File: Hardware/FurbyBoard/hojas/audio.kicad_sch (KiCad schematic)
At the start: 8 parts, among them J5 Micro I2S (3V3, GND, SCK, WS,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, U7 MAX98357AETE+T

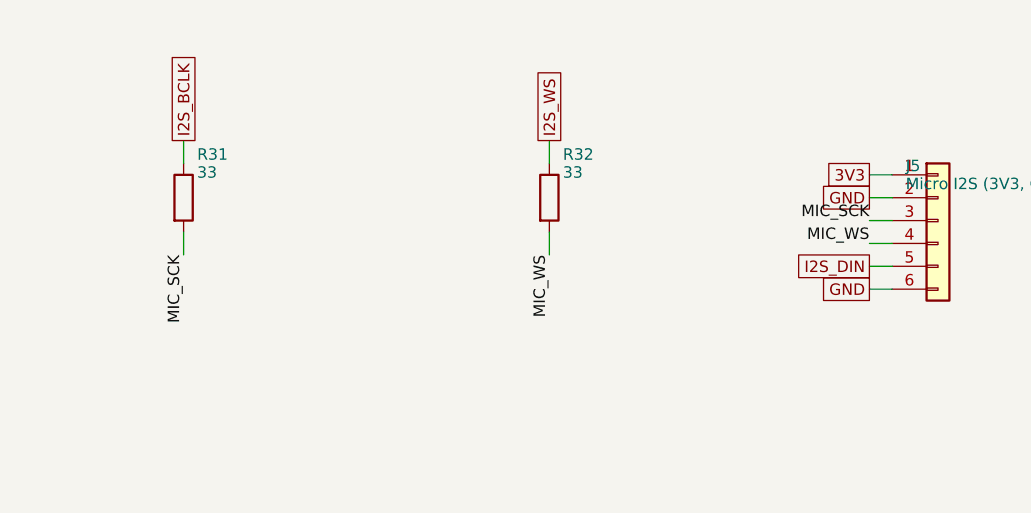
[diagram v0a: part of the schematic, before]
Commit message: Refactor: pads de cable agrupados por zona y etiquetas globales
- Motor en J9 con leva, encoder y sensores; altavoz en J8 con inclinación y
  lengua; luz en J7 con el IR. Desaparecen J4 y J10: cada grupo sale por el
  borde más cercano a su destino.
- Micro en 2x03 en vez de 1x06 para que quepa junto al borde derecho.
- Todas las etiquetas del esquemático son globales, así el nombre de red
  coincide con el del PCB (paridad sin prefijos de hoja).
- ERC 0 errores, 0 avisos.

Co-Authored-By: Claude Opus 5.5 (1M context) <noreply@anthropic.com>
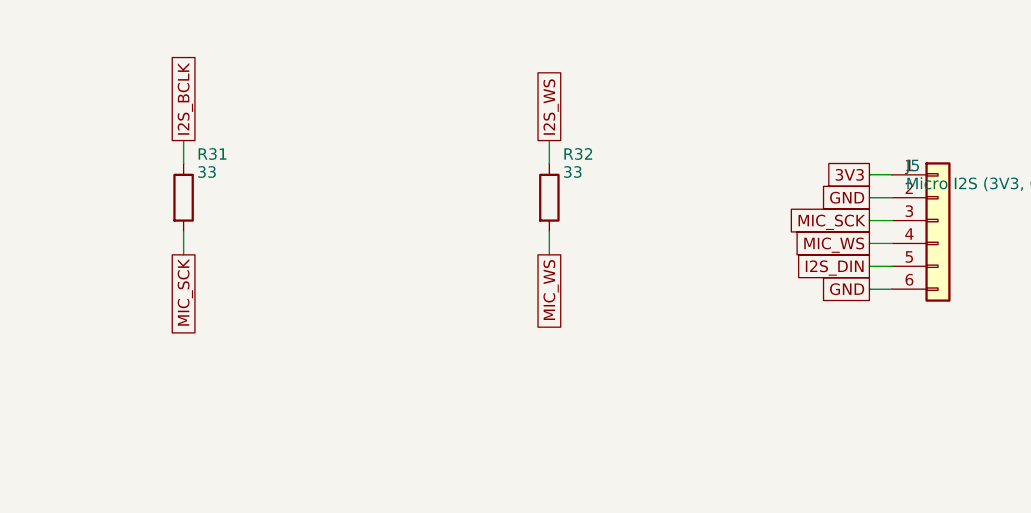
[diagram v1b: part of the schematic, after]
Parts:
- J5: footprint FurbyBoard:Pads_1x06_P2.54mm -> FurbyBoard:Pads_2x03_P2.54mm

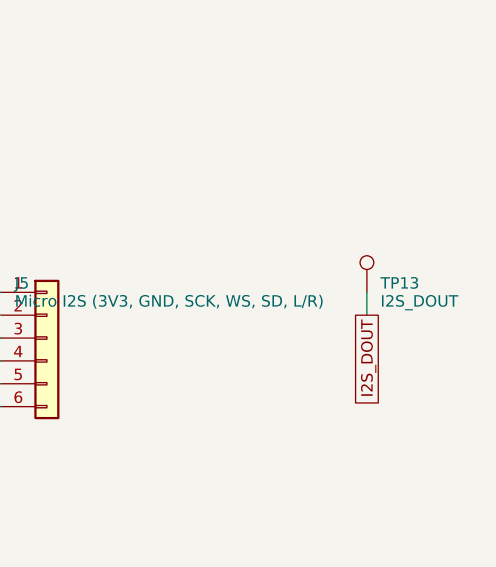
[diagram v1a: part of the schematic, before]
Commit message: Feature: par USB trazado, planos GND/VSYS y serigrafía de la FurbyBoard
- Par USB de J1 al ESD y al módulo, acoplado 0,28/0,15 por F.Cu sobre el
  plano de GND, sin vías (rutas_fijas.py, bloqueado para el autorrutado).
  Canal libre en x -83 bajo la batería.
- In1 plano de GND e In2 plano de VSYS; potencia por pista a 0,4 (cabe en
  los pads de 0,5 de paso) y 3V3 a 0,3. exportar_dsn.py deja el DSN para
  Freerouting con las clases de red.
- Rótulos de serigrafía colocados solos (serigrafia.py): TP, LED, botones,
  puentes y polaridad de la batería arriba; función de cada pad de cable y
  GPIO del J_EXP abajo, con leyenda para J7, J9 y J5.
- Para que quepan los rótulos: fila de LED con resistencias debajo, botones
  en vertical, rejilla de TP con el rótulo debajo. Quedan 14 TP: fuera EN e
  IO0 (se miden en los pads de SW1 y SW2), CHG y PG (en D1 y D2) y un GND.

ERC 0/0. DRC 0 salvo una vía de GND sin plano relleno; sin rutar.

Co-Authored-By: Claude Opus 5.5 (1M context) <noreply@anthropic.com>
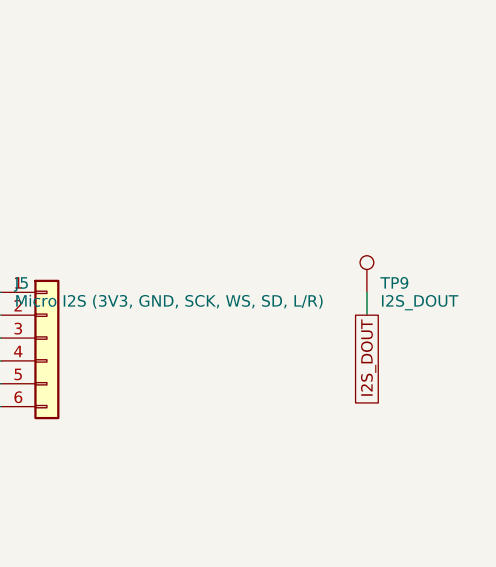
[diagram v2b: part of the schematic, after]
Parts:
- removed TP13: I2S_DOUT, TestPoint:TestPoint_Pad_D1.5mm, symbol Connector:TestPoint
- added TP9: I2S_DOUT, TestPoint:TestPoint_Pad_D1.5mm, symbol Connector:TestPoint
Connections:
- net I2S_DOUT: now also TP9.1
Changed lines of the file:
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@@
-	)
-	(symbol
-		(lib_id "Connector:TestPoint")
-		(at 353.06 66.04 0)
-		(unit 1)
-		(body_style 1)
-		(exclude_from_sim no)
-		(in_bom no)
-		(on_board yes)
-		(in_pos_files yes)
-		(dnp no)
-		(property "Reference" "TP13"
-			(at 354.56 65.04 0)
-			(show_name no)
-			(do_not_autoplace no)
-			(effects
-				(font
-					(size 1.27 1.27)
-				)
-				(justify left)
-			)
-		)
-		(property "Value" "I2S_DOUT"
-			(at 354.56 67.04 0)
-			(show_name no)
-			(do_not_autoplace no)
-			(effects
-				(font
-					(size 1.27 1.27)
-				)
-				(justify left)
-			)
-		)
-		(property "Footprint" "TestPoint:TestPoint_Pad_D1.5mm"
-			(at 353.06 66.04 0)
-			(hide yes)
-			(show_name no)
-			(do_not_autoplace no)
-			(effects
-				(font
-					(size 1.27 1.27)
-				)
-				(justify left)
-			)
-		)
-		(property "Datasheet" ""
-			(at 353.06 66.04 0)
-			(hide yes)
-			(show_name no)
-			(do_not_autoplace no)
-			(effects
-				(font
-					(size 1.27 1.27)
-				)
-				(justify left)
-			)
-		)
-		(property "Description" "Datos I2S al amplificador"
-			(at 353.06 66.04 0)
-			(hide yes)
-			(show_name no)
-			(do_not_autoplace no)
-			(effects
-				(font
-					(size 1.27 1.27)
-				)
-				(justify left)
-			)
-		)
-		(property "LCSC" ""
-			(at 353.06 66.04 0)
-			(hide yes)
-			(show_name no)
-			(do_not_autoplace no)
-			(effects
-				(font
-					(size 1.27 1.27)
-				)
-				(justify left)
-			)
-		)
-		(property "JLC_Class" ""
-			(at 353.06 66.04 0)
-			(hide yes)
-			(show_name no)
-			(do_not_autoplace no)
-			(effects
-				(font
-					(size 1.27 1.27)
-				)
-				(justify left)
-			)
-		)
-		(property "MPN" ""
-			(at 353.06 66.04 0)
-			(hide yes)
-			(show_name no)
-			(do_not_autoplace no)
-			(effects
-				(font
-					(size 1.27 1.27)
-				)
-				(justify left)
-			)
-		)
-		(pin "1"
-		)
-		(instances
-			(project "FurbyBoard"
-				(path "/8b4f1e2a-3c5d-4e6f-9a1b-2c3d4e5f6a7b/259e0c7a-58f0-5f84-8b75-920a4cd1054d"
-					(reference "TP13")
-					(unit 1)
-				)
-			)
-		)
 	)
 	(symbol
@@
 					(unit 1)
 				)
+			)
+		)
+	)
+	(symbol
+		(lib_id "Connector:TestPoint")
+		(at 353.06 66.04 0)
+		(unit 1)
+		(body_style 1)
+		(exclude_from_sim no)
+		(in_bom no)
+		(on_board yes)
+		(in_pos_files yes)
+		(dnp no)
+		(property "Reference" "TP9"
+			(at 354.56 65.04 0)
+			(show_name no)
+			(do_not_autoplace no)
+			(effects
+				(font
+					(size 1.27 1.27)
+				)
+				(justify left)
+			)
+		)
+		(property "Value" "I2S_DOUT"
+			(at 354.56 67.04 0)
+			(show_name no)
+			(do_not_autoplace no)
+			(effects
+				(font
+					(size 1.27 1.27)
+				)
+				(justify left)
+			)
+		)
+		(property "Footprint" "TestPoint:TestPoint_Pad_D1.5mm"
+			(at 353.06 66.04 0)
+			(hide yes)
+			(show_name no)
+			(do_not_autoplace no)
+			(effects
+				(font
+					(size 1.27 1.27)
+				)
+				(justify left)
+			)
+		)
+		(property "Datasheet" ""
+			(at 353.06 66.04 0)
+			(hide yes)
+			(show_name no)
+			(do_not_autoplace no)
+			(effects
+				(font
+					(size 1.27 1.27)
+				)
+				(justify left)
+			)
+		)
+		(property "Description" "Datos I2S al amplificador"
+			(at 353.06 66.04 0)
+			(hide yes)
+			(show_name no)
+			(do_not_autoplace no)
+			(effects
+				(font
+					(size 1.27 1.27)
+				)
+				(justify left)
+			)
+		)
+		(property "LCSC" ""
+			(at 353.06 66.04 0)
+			(hide yes)
+			(show_name no)
+			(do_not_autoplace no)
+			(effects
+				(font
+					(size 1.27 1.27)
+				)
+				(justify left)
+			)
+		)
+		(property "JLC_Class" ""
+			(at 353.06 66.04 0)
+			(hide yes)
+			(show_name no)
+			(do_not_autoplace no)
+			(effects
+				(font
+					(size 1.27 1.27)
+				)
+				(justify left)
+			)
+		)
+		(property "MPN" ""
+			(at 353.06 66.04 0)
+			(hide yes)
+			(show_name no)
+			(do_not_autoplace no)
+			(effects
+				(font
+					(size 1.27 1.27)
+				)
+				(justify left)
+			)
+		)
+		(pin "1"
+		)
+		(instances
+			(project "FurbyBoard"
+				(path "/8b4f1e2a-3c5d-4e6f-9a1b-2c3d4e5f6a7b/259e0c7a-58f0-5f84-8b75-920a4cd1054d"
+					(reference "TP9")
+					(unit 1)
+				)

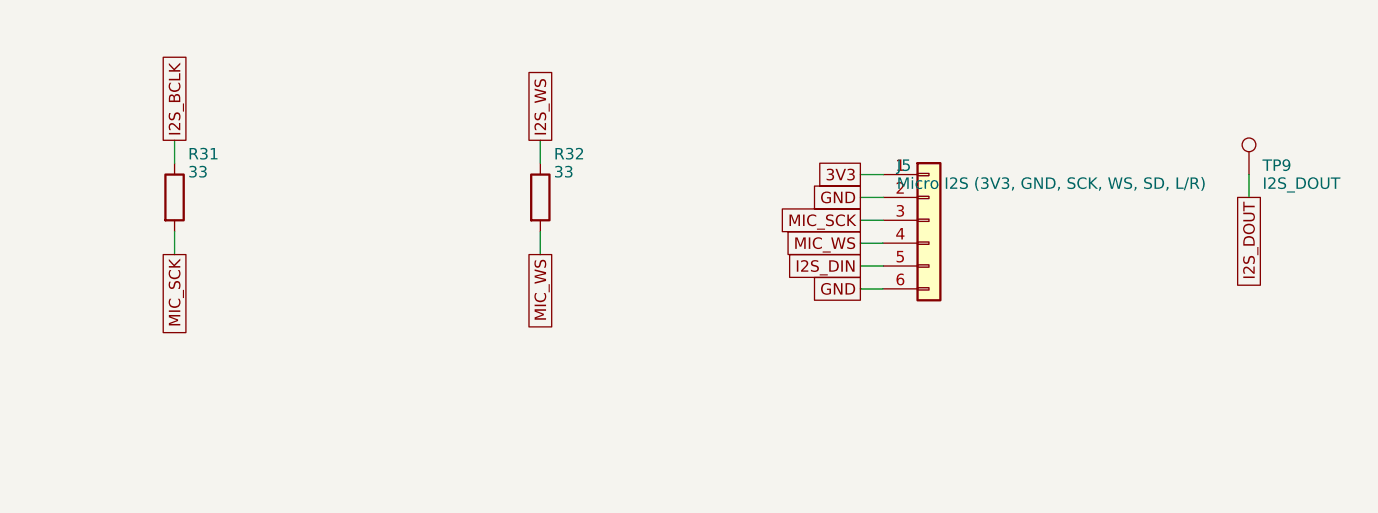
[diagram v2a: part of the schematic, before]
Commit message: Feature: esquema de la FurbyBoard al procedimiento nuevo: rúbrica L, reglas por red, pines por geometría y simulación del elevador
- Rúbrica S/M/L (L) y tabla de raíles con anchos mínimos (params.ANCHOS_MINIMOS), que gen_pro.py vuelca al .kicad_dru como una regla por red, con cuellos dentro de los patios de los QFN y de J1.
- Vías de 0,45/0,2 solo en la clase USB (cruce del par en el receptáculo de 16 pines); el resto sigue en 0,6/0,3.
- pcb-toolkit.toml: clases B/C/D, anchos, grupos explícitos y zonas del puente H y de la clase D.
- Redes a la convención: BB_SW1/2, I2S_SCK_MIC/I2S_WS_MIC.
- Pines del módulo (I2S, HOME, EXP_INT) y puertos del TCA9535 por geometría, sin tocar strapping, USB ni ADC.
- LED del encoder desde V6 por 470 ohm (sin Q2); J_EXP 2x5; J9 y J5 reordenados; serigrafía al día.
- ERC 0/0. Simulación ngspice del elevador en el peor caso (sim/). Informes de las puertas A y B en revisiones/; un crítico (NTC del cargador) queda escalado.

Co-Authored-By: Claude Fable 5.1 <noreply@anthropic.com>
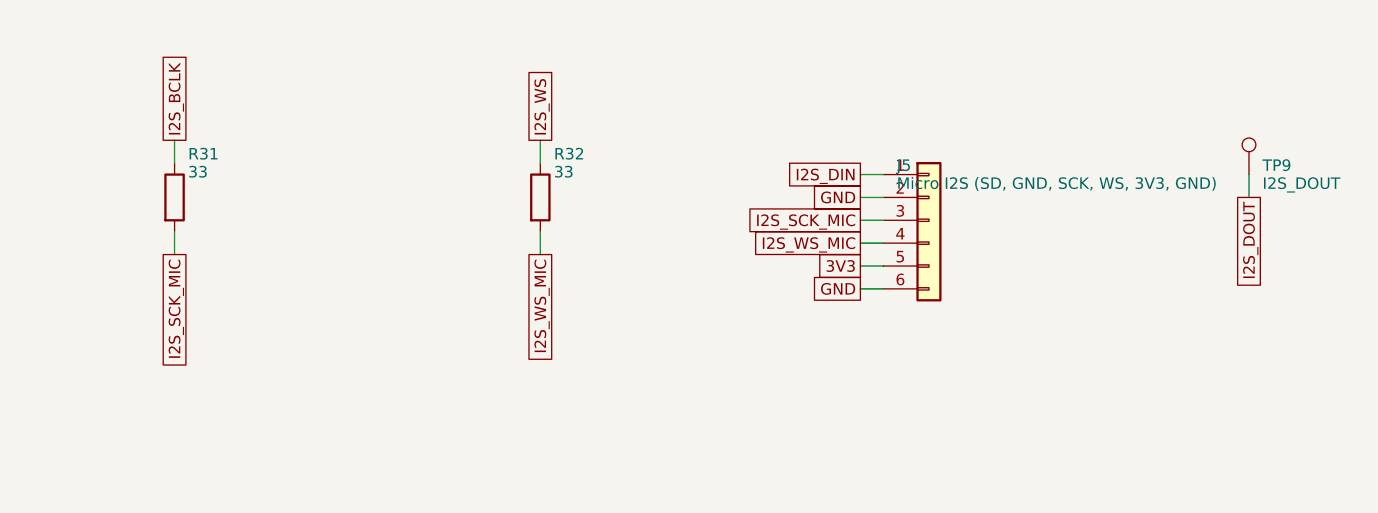
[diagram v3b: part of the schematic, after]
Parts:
- J5: value Micro I2S (3V3, GND, SCK, WS, SD, L/R) -> Micro I2S (SD, GND, SCK, WS, 3V3, GND)
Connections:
- net 3V3: now also J5.5 (Pin_5); no longer J5.1 (Pin_1)
- net I2S_DIN: now also J5.1 (Pin_1); no longer J5.5 (Pin_5)
- net MIC_SCK renamed I2S_SCK_MIC
- net MIC_WS renamed I2S_WS_MIC
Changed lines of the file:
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@@
 		)
 	)
-	(global_label "MIC_SCK"
+	(global_label "I2S_SCK_MIC"
 		(shape passive)
 		(at 233.68 74.93 270)
@@
 		)
 	)
-	(global_label "MIC_SCK"
+	(global_label "I2S_SCK_MIC"
 		(shape passive)
 		(at 309.88 71.12 180)
@@
 		)
 	)
-	(global_label "MIC_WS"
+	(global_label "I2S_WS_MIC"
 		(shape passive)
 		(at 274.32 74.93 270)
@@
 		)
 	)
-	(global_label "MIC_WS"
+	(global_label "I2S_WS_MIC"
 		(shape passive)
 		(at 309.88 73.66 180)
@@
 		)
 	)
+	(global_label "3V3"
+		(shape passive)
+		(at 309.88 76.2 180)
+		(fields_autoplaced yes)
+		(effects
+			(font
+				(size 1.27 1.27)
+			)
+			(justify right)
+		)
+		(property "Intersheetrefs" "${INTERSHEET_REFS}"
+			(at 309.88 76.2 0)
+			(hide yes)
+			(show_name no)
+			(do_not_autoplace no)
+			(effects
+				(font
+					(size 1.27 1.27)
+				)
+			)
+		)
+	)
+	(global_label "VSYS"
+		(shape passive)
+		(at 60.96 63.5 90)
+		(fields_autoplaced yes)
+		(effects
+			(font
+				(size 1.27 1.27)
+			)
+			(justify left)
+		)
+		(property "Intersheetrefs" "${INTERSHEET_REFS}"
+			(at 60.96 63.5 0)
+			(hide yes)
+			(show_name no)
+			(do_not_autoplace no)
+			(effects
+				(font
+					(size 1.27 1.27)
+				)
+			)
+		)
+	)
+	(global_label "VSYS"
+		(shape passive)
+		(at 60.96 63.5 90)
+		(fields_autoplaced yes)
+		(effects
+			(font
+				(size 1.27 1.27)
+			)
+			(justify left)
+		)
+		(property "Intersheetrefs" "${INTERSHEET_REFS}"
+			(at 60.96 63.5 0)
+			(hide yes)
+			(show_name no)
+			(do_not_autoplace no)
+			(effects
+				(font
+					(size 1.27 1.27)
+				)
+			)
+		)
+	)
+	(global_label "I2S_WS"
+		(shape passive)
+		(at 274.32 62.23 90)
+		(fields_autoplaced yes)
+		(effects
+			(font
+				(size 1.27 1.27)
+			)
+			(justify left)
+		)
+		(property "Intersheetrefs" "${INTERSHEET_REFS}"
+			(at 274.32 62.23 0)
+			(hide yes)
+			(show_name no)
+			(do_not_autoplace no)
+			(effects
+				(font
+					(size 1.27 1.27)
+				)
+			)
+		)
+	)
+	(global_label "I2S_DOUT"
+		(shape passive)
+		(at 45.72 71.12 180)
+		(fields_autoplaced yes)
+		(effects
+			(font
+				(size 1.27 1.27)
+			)
+			(justify right)
+		)
+		(property "Intersheetrefs" "${INTERSHEET_REFS}"
+			(at 45.72 71.12 0)
+			(hide yes)
+			(show_name no)
+			(do_not_autoplace no)
+			(effects
+				(font
+					(size 1.27 1.27)
+				)
+			)
+		)
+	)
+	(global_label "I2S_WS"
+		(shape passive)
+		(at 45.72 76.2 180)
+		(fields_autoplaced yes)
+		(effects
+			(font
+				(size 1.27 1.27)
+			)
+			(justify right)
+		)
+		(property "Intersheetrefs" "${INTERSHEET_REFS}"
+			(at 45.72 76.2 0)
+			(hide yes)
+			(show_name no)
+			(do_not_autoplace no)
+			(effects
+				(font
+					(size 1.27 1.27)
+				)
+			)
+		)
+	)
 	(global_label "I2S_DIN"
-		(shape passive)
-		(at 309.88 76.2 180)
-		(fields_autoplaced yes)
-		(effects
-			(font
-				(size 1.27 1.27)
-			)
-			(justify right)
-		)
-		(property "Intersheetrefs" "${INTERSHEET_REFS}"
-			(at 309.88 76.2 0)
-			(hide yes)
-			(show_name no)
-			(do_not_autoplace no)
-			(effects
-				(font
-					(size 1.27 1.27)
-				)
-			)
-		)
-	)
-	(global_label "VSYS"
-		(shape passive)
-		(at 60.96 63.5 90)
-		(fields_autoplaced yes)
-		(effects
-			(font
-				(size 1.27 1.27)
-			)
-			(justify left)
-		)
-		(property "Intersheetrefs" "${INTERSHEET_REFS}"
-			(at 60.96 63.5 0)
-			(hide yes)
-			(show_name no)
-			(do_not_autoplace no)
-			(effects
-				(font
-					(size 1.27 1.27)
-				)
-			)
-		)
-	)
-	(global_label "VSYS"
-		(shape passive)
-		(at 60.96 63.5 90)
-		(fields_autoplaced yes)
-		(effects
-			(font
-				(size 1.27 1.27)
-			)
-			(justify left)
-		)
-		(property "Intersheetrefs" "${INTERSHEET_REFS}"
-			(at 60.96 63.5 0)
-			(hide yes)
-			(show_name no)
-			(do_not_autoplace no)
-			(effects
-				(font
-					(size 1.27 1.27)
-				)
-			)
-		)
-	)
-	(global_label "I2S_WS"
-		(shape passive)
-		(at 274.32 62.23 90)
-		(fields_autoplaced yes)
-		(effects
-			(font
-				(size 1.27 1.27)
-			)
-			(justify left)
-		)
-		(property "Intersheetrefs" "${INTERSHEET_REFS}"
-			(at 274.32 62.23 0)
-			(hide yes)
-			(show_name no)
-			(do_not_autoplace no)
-			(effects
-				(font
-					(size 1.27 1.27)
-				)
-			)
-		)
-	)
-	(global_label "I2S_DOUT"
-		(shape passive)
-		(at 45.72 71.12 180)
-		(fields_autoplaced yes)
-		(effects
-			(font
-				(size 1.27 1.27)
-			)
-			(justify right)
-		)
-		(property "Intersheetrefs" "${INTERSHEET_REFS}"
-			(at 45.72 71.12 0)
-			(hide yes)
-			(show_name no)
-			(do_not_autoplace no)
-			(effects
-				(font
-					(size 1.27 1.27)
-				)
-			)
-		)
-	)
-	(global_label "I2S_WS"
-		(shape passive)
-		(at 45.72 76.2 180)
-		(fields_autoplaced yes)
-		(effects
-			(font
-				(size 1.27 1.27)
-			)
-			(justify right)
-		)
-		(property "Intersheetrefs" "${INTERSHEET_REFS}"
-			(at 45.72 76.2 0)
-			(hide yes)
-			(show_name no)
-			(do_not_autoplace no)
-			(effects
-				(font
-					(size 1.27 1.27)
-				)
-			)
-		)
-	)
-	(global_label "3V3"
 		(shape passive)
 		(at 309.88 66.04 180)
@@
 			)
 		)
-		(property "Value" "Micro I2S (3V3, GND, SCK, WS, SD, L/R)"
+		(property "Value" "Micro I2S (SD, GND, SCK, WS, 3V3, GND)"
 			(at 313.92 67.04 0)
 			(show_name no)
@@
 			)
 		)
-		(property "Description" "Micro I2S (3V3, GND, SCK, WS, SD, L/R)"
+		(property "Description" "Micro I2S (SD, GND, SCK, WS, 3V3, GND)"
 			(at 317.5 71.12 0)
 			(hide yes)

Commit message: Fix: C41 de 10 µF junto a VDD de U7 y R57/R58 a 1 kΩ (arreglos de la simulación)
- C41 (C19702, 10 µF 10 V X5R 0603) al oeste de C26, a 1,3 mm de los pines 7/8,
  del lado de los pines del puente de VSYS de B.Cu; VSYS al tronco de los pines
  (0,6 mm, y -86,075) y GND por su vía al oeste. sim: 257 mV pp en VDD con solo C26.
- Micromovimientos: vía de TONGUE_PAD 0,7 mm al norte (diagonal desde R44.2; B.Cu por
  y -83,55) y segunda vía de VSYS del puente de x -97,0 a -96,875 (baja en F.Cu al
  tramo de C41). Ni I2S ni salidas al altavoz tocados.
- R57 y R58 de 2,2 kΩ / 1,5 kΩ a 1 kΩ (C21190): D4/D5 son verdes InGaN (2,6–3,1 V).

Puertas: ERC 0; DRC con paridad 0 infracciones, 0 sin unir; revisar-rutado PASS
(0 errores, los mismos 152 avisos que antes); rellenos sin islas nuevas (GND In1/In4
3279,4 mm² en 1, F 2055,0 en 21, B 2758,1 en 11; VSYS In2 2583,6 en 3).
PNG revisados: F.Cu, B.Cu, In2 y cobre de la ventana de U7/C41/R44 (10 × 10 mm).

Co-Authored-By: Claude Opus 5.5 (1M context) <noreply@anthropic.com>
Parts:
- added C41: 10u, Capacitor_SMD:C_0603_1608Metric, symbol Device:C
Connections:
- net GND: now also C41.2
- net VSYS: now also C41.1
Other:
- note added: "VDD: C26 (100 nF) y C41 (10 µF) junto a los pines 7/8; C24/C25 (22 µF) al otro lado del puente de VSYS."
- moved on the sheet: J5, R31, R32, TP9
